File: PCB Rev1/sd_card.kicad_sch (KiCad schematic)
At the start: 5 parts, among them J4 MICRO_SD

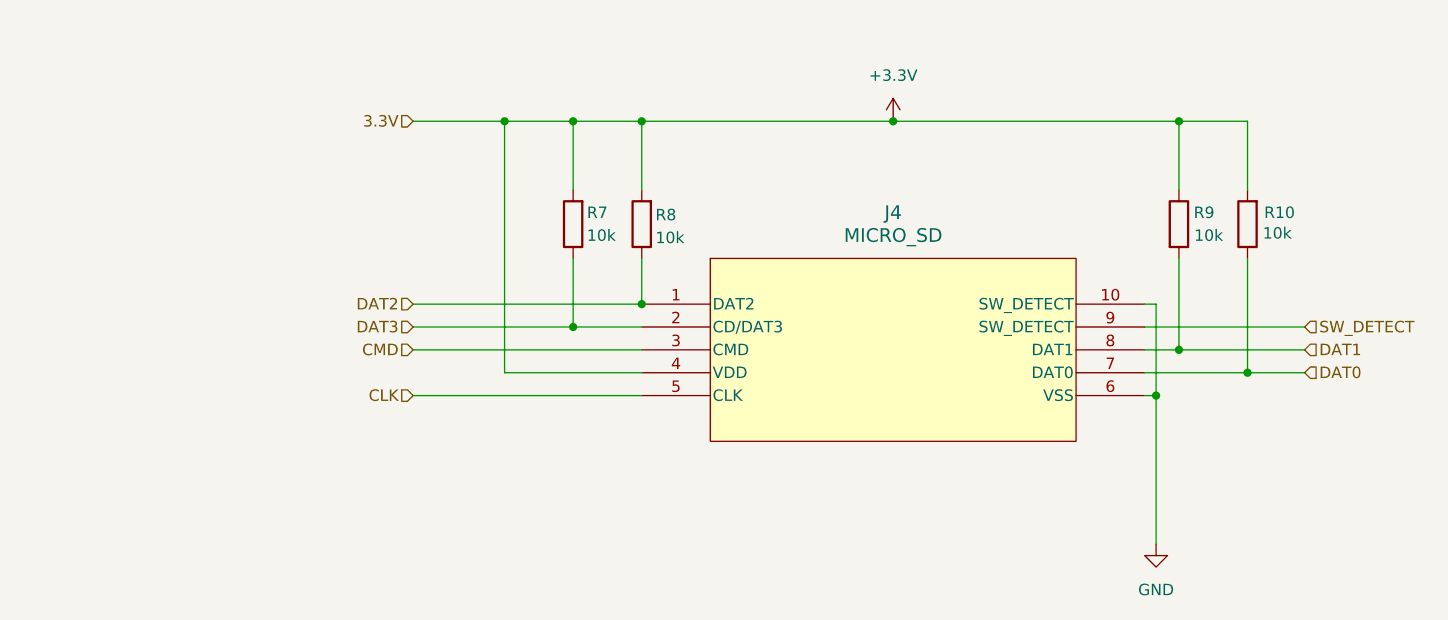
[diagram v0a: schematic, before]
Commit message: rev 2 schematic with minor changes, final send out before layout
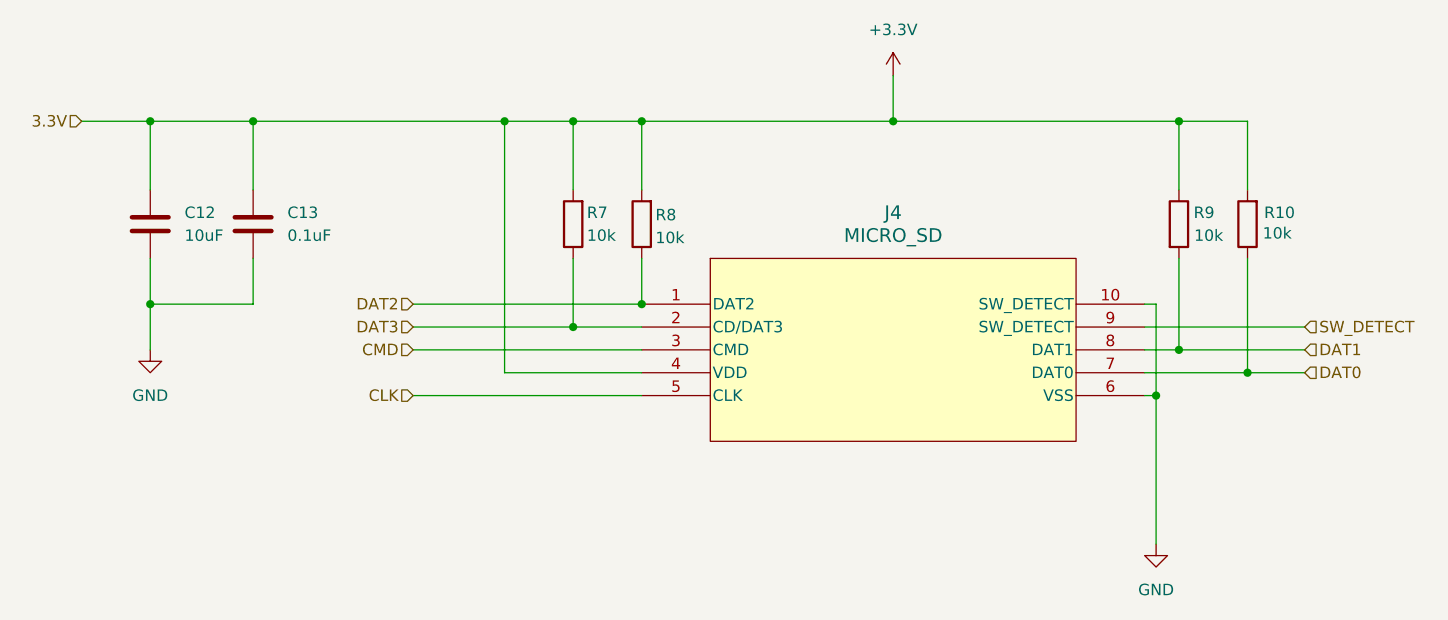
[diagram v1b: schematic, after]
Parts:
- added C12: 10uF, symbol Device:C
- added C13: 0.1uF, symbol Device:C
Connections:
- net +3.3V: now also C12.1, C13.1
- net GND: now also C12.2, C13.2
